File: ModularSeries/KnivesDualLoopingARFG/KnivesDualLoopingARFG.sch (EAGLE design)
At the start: 74 parts, among them P1 2XWIREPAD, P2 2XWIREPAD, P3 2XWIREPAD, P4 2XWIREPAD, Q1 2N3904, Q2 2N3904

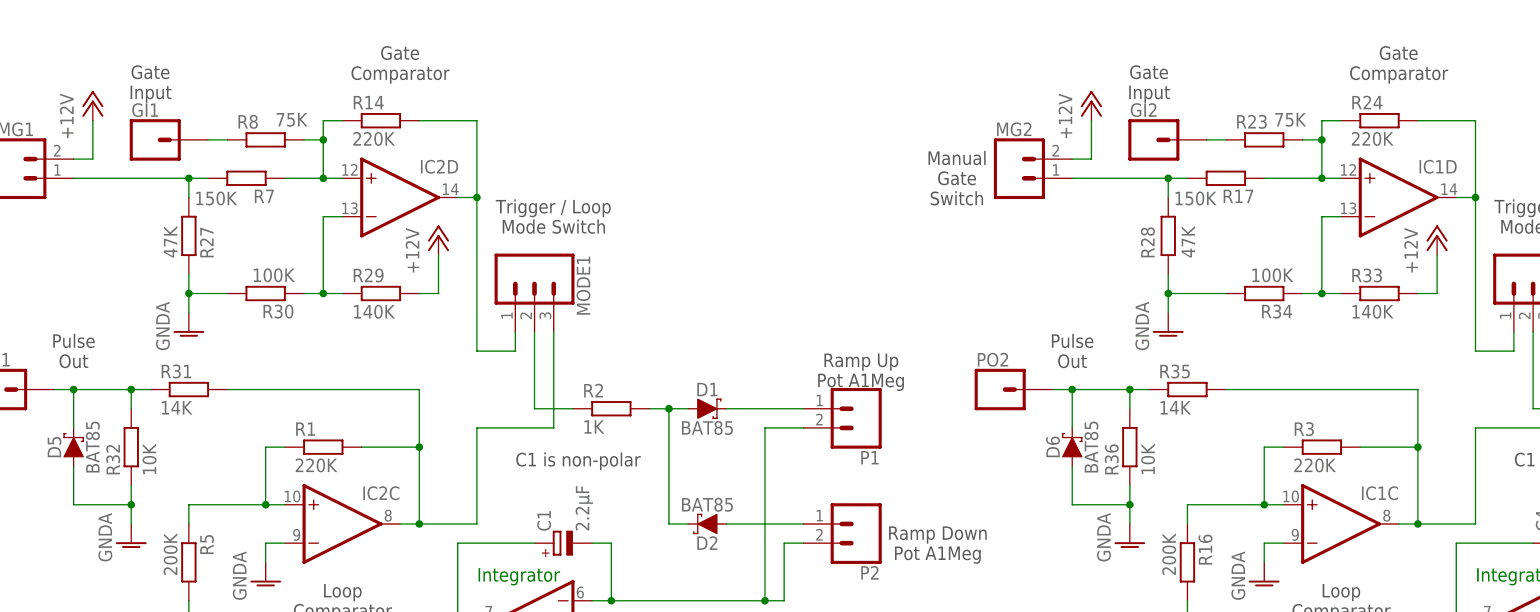
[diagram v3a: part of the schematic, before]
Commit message: Updates to Portals and Knives, Panel layout for Prism and Knives added
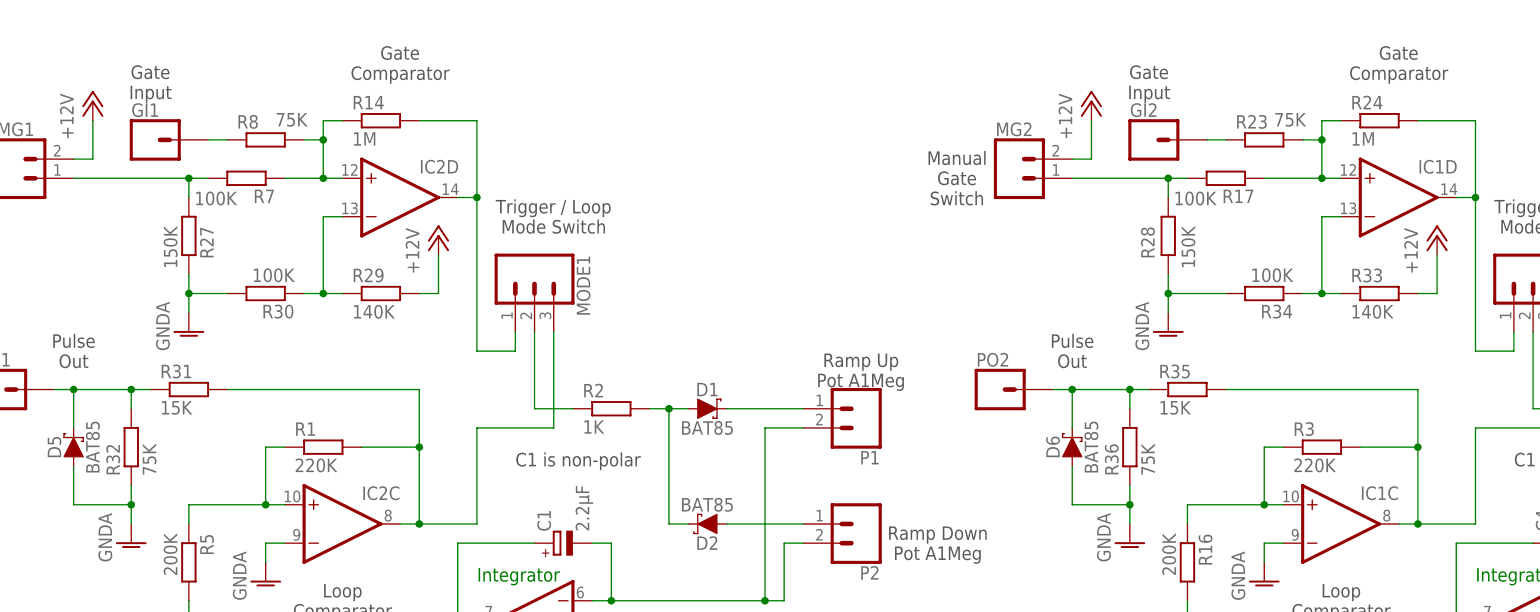
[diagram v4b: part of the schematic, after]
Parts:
- R14, R24: value 220K -> 1M
- R17, R7: value 150K -> 100K
- R27, R28: value 47K -> 150K
- R31, R35: value 14K -> 15K
- R32, R36: value 10K -> 75K
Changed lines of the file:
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@@
 <part name="R2" library="rcl" library_urn="urn:adsk.eagle:library:334" deviceset="R-EU_" device="0207/10" package3d_urn="urn:adsk.eagle:package:23491/2" value="1K"/>
 <part name="R5" library="rcl" library_urn="urn:adsk.eagle:library:334" deviceset="R-EU_" device="0207/10" package3d_urn="urn:adsk.eagle:package:23491/2" value="200K"/>
-<part name="R7" library="rcl" library_urn="urn:adsk.eagle:library:334" deviceset="R-EU_" device="0207/10" package3d_urn="urn:adsk.eagle:package:23491/2" value="150K"/>
+<part name="R7" library="rcl" library_urn="urn:adsk.eagle:library:334" deviceset="R-EU_" device="0207/10" package3d_urn="urn:adsk.eagle:package:23491/2" value="100K"/>
 <part name="R9" library="rcl" library_urn="urn:adsk.eagle:library:334" deviceset="R-EU_" device="0207/10" package3d_urn="urn:adsk.eagle:package:23491/2" value="100K"/>
 <part name="R10" library="rcl" library_urn="urn:adsk.eagle:library:334" deviceset="R-EU_" device="0207/10" package3d_urn="urn:adsk.eagle:package:23491/2" value="47K"/>
@@
 <part name="R8" library="rcl" library_urn="urn:adsk.eagle:library:334" deviceset="R-EU_" device="0207/10" package3d_urn="urn:adsk.eagle:package:23491/2" value="75K"/>
 <part name="P+2" library="supply1" library_urn="urn:adsk.eagle:library:371" deviceset="+12V" device=""/>
-<part name="R14" library="rcl" library_urn="urn:adsk.eagle:library:334" deviceset="R-EU_" device="0207/10" package3d_urn="urn:adsk.eagle:package:23491/2" value="220K"/>
+<part name="R14" library="rcl" library_urn="urn:adsk.eagle:library:334" deviceset="R-EU_" device="0207/10" package3d_urn="urn:adsk.eagle:package:23491/2" value="1M"/>
 <part name="Q1" library="transistor" library_urn="urn:adsk.eagle:library:402" deviceset="2N3904" device="" package3d_urn="urn:adsk.eagle:package:28523/2" value="2N3904"/>
 <part name="R6" library="rcl" library_urn="urn:adsk.eagle:library:334" deviceset="R-EU_" device="0207/10" package3d_urn="urn:adsk.eagle:package:23491/2" value="100Ω"/>
@@
 <part name="R4" library="rcl" library_urn="urn:adsk.eagle:library:334" deviceset="R-EU_" device="0207/10" package3d_urn="urn:adsk.eagle:package:23491/2" value="1K"/>
 <part name="R16" library="rcl" library_urn="urn:adsk.eagle:library:334" deviceset="R-EU_" device="0207/10" package3d_urn="urn:adsk.eagle:package:23491/2" value="200K"/>
-<part name="R17" library="rcl" library_urn="urn:adsk.eagle:library:334" deviceset="R-EU_" device="0207/10" package3d_urn="urn:adsk.eagle:package:23491/2" value="150K"/>
+<part name="R17" library="rcl" library_urn="urn:adsk.eagle:library:334" deviceset="R-EU_" device="0207/10" package3d_urn="urn:adsk.eagle:package:23491/2" value="100K"/>
 <part name="R18" library="rcl" library_urn="urn:adsk.eagle:library:334" deviceset="R-EU_" device="0207/10" package3d_urn="urn:adsk.eagle:package:23491/2" value="100K"/>
 <part name="R19" library="rcl" library_urn="urn:adsk.eagle:library:334" deviceset="R-EU_" device="0207/10" package3d_urn="urn:adsk.eagle:package:23491/2" value="47K"/>
@@
 <part name="R23" library="rcl" library_urn="urn:adsk.eagle:library:334" deviceset="R-EU_" device="0207/10" package3d_urn="urn:adsk.eagle:package:23491/2" value="75K"/>
 <part name="P+5" library="supply1" library_urn="urn:adsk.eagle:library:371" deviceset="+12V" device=""/>
-<part name="R24" library="rcl" library_urn="urn:adsk.eagle:library:334" deviceset="R-EU_" device="0207/10" package3d_urn="urn:adsk.eagle:package:23491/2" value="220K"/>
+<part name="R24" library="rcl" library_urn="urn:adsk.eagle:library:334" deviceset="R-EU_" device="0207/10" package3d_urn="urn:adsk.eagle:package:23491/2" value="1M"/>
 <part name="GND11" library="supply1" library_urn="urn:adsk.eagle:library:371" deviceset="GNDA" device=""/>
 <part name="Q2" library="transistor" library_urn="urn:adsk.eagle:library:402" deviceset="2N3904" device="" package3d_urn="urn:adsk.eagle:package:28523/2" value="2N3904"/>
@@
 <part name="H3" library="holes" library_urn="urn:adsk.eagle:library:237" deviceset="MOUNT-HOLE" device="3.2" package3d_urn="urn:adsk.eagle:package:14275/1"/>
 <part name="H4" library="holes" library_urn="urn:adsk.eagle:library:237" deviceset="MOUNT-HOLE" device="3.2" package3d_urn="urn:adsk.eagle:package:14275/1"/>
-<part name="R27" library="rcl" library_urn="urn:adsk.eagle:library:334" deviceset="R-EU_" device="0207/10" package3d_urn="urn:adsk.eagle:package:23491/2" value="47K"/>
-<part name="R28" library="rcl" library_urn="urn:adsk.eagle:library:334" deviceset="R-EU_" device="0207/10" package3d_urn="urn:adsk.eagle:package:23491/2" value="47K"/>
+<part name="R27" library="rcl" library_urn="urn:adsk.eagle:library:334" deviceset="R-EU_" device="0207/10" package3d_urn="urn:adsk.eagle:package:23491/2" value="150K"/>
+<part name="R28" library="rcl" library_urn="urn:adsk.eagle:library:334" deviceset="R-EU_" device="0207/10" package3d_urn="urn:adsk.eagle:package:23491/2" value="150K"/>
 <part name="PO1" library="ElectricNoodleBox" deviceset="1XWIREPAD" device=""/>
 <part name="PO2" library="ElectricNoodleBox" deviceset="1XWIREPAD" device=""/>
@@
 <attribute name="SPICEPREFIX" value="G"/>
 </part>
-<part name="R31" library="rcl" library_urn="urn:adsk.eagle:library:334" deviceset="R-EU_" device="0207/10" package3d_urn="urn:adsk.eagle:package:23491/2" value="14K"/>
-<part name="R32" library="rcl" library_urn="urn:adsk.eagle:library:334" deviceset="R-EU_" device="0207/10" package3d_urn="urn:adsk.eagle:package:23491/2" value="10K"/>
+<part name="R31" library="rcl" library_urn="urn:adsk.eagle:library:334" deviceset="R-EU_" device="0207/10" package3d_urn="urn:adsk.eagle:package:23491/2" value="15K"/>
+<part name="R32" library="rcl" library_urn="urn:adsk.eagle:library:334" deviceset="R-EU_" device="0207/10" package3d_urn="urn:adsk.eagle:package:23491/2" value="75K"/>
 <part name="GND15" library="supply1" library_urn="urn:adsk.eagle:library:371" deviceset="GNDA" device=""/>
 <part name="D5" library="ElectricNoodleBox" deviceset="SCHOTTKY_DO35" device="" package3d_urn="urn:adsk.eagle:package:43339/2" value="BAT85"/>
@@
 <part name="R33" library="rcl" library_urn="urn:adsk.eagle:library:334" deviceset="R-EU_" device="0207/10" package3d_urn="urn:adsk.eagle:package:23491/2" value="140K"/>
 <part name="R34" library="rcl" library_urn="urn:adsk.eagle:library:334" deviceset="R-EU_" device="0207/10" package3d_urn="urn:adsk.eagle:package:23491/2" value="100K"/>
-<part name="R35" library="rcl" library_urn="urn:adsk.eagle:library:334" deviceset="R-EU_" device="0207/10" package3d_urn="urn:adsk.eagle:package:23491/2" value="14K"/>
-<part name="R36" library="rcl" library_urn="urn:adsk.eagle:library:334" deviceset="R-EU_" device="0207/10" package3d_urn="urn:adsk.eagle:package:23491/2" value="10K"/>
+<part name="R35" library="rcl" library_urn="urn:adsk.eagle:library:334" deviceset="R-EU_" device="0207/10" package3d_urn="urn:adsk.eagle:package:23491/2" value="15K"/>
+<part name="R36" library="rcl" library_urn="urn:adsk.eagle:library:334" deviceset="R-EU_" device="0207/10" package3d_urn="urn:adsk.eagle:package:23491/2" value="75K"/>
 <part name="GND5" library="supply1" library_urn="urn:adsk.eagle:library:371" deviceset="GNDA" device=""/>
 <part name="D6" library="ElectricNoodleBox" deviceset="SCHOTTKY_DO35" device="" package3d_urn="urn:adsk.eagle:package:43339/2" value="BAT85"/>

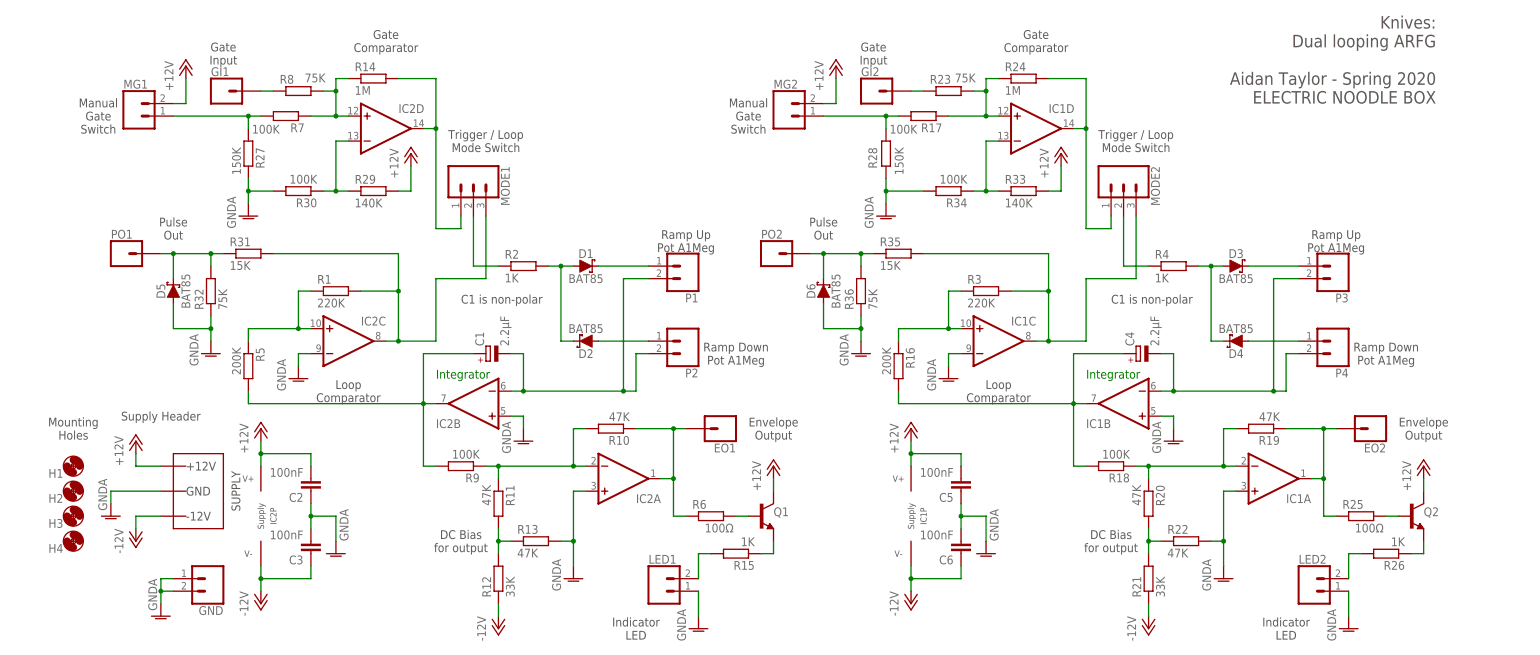
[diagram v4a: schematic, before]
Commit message: Pulse output fixed on Knives, schematics and layout updated. Panel added for Portals
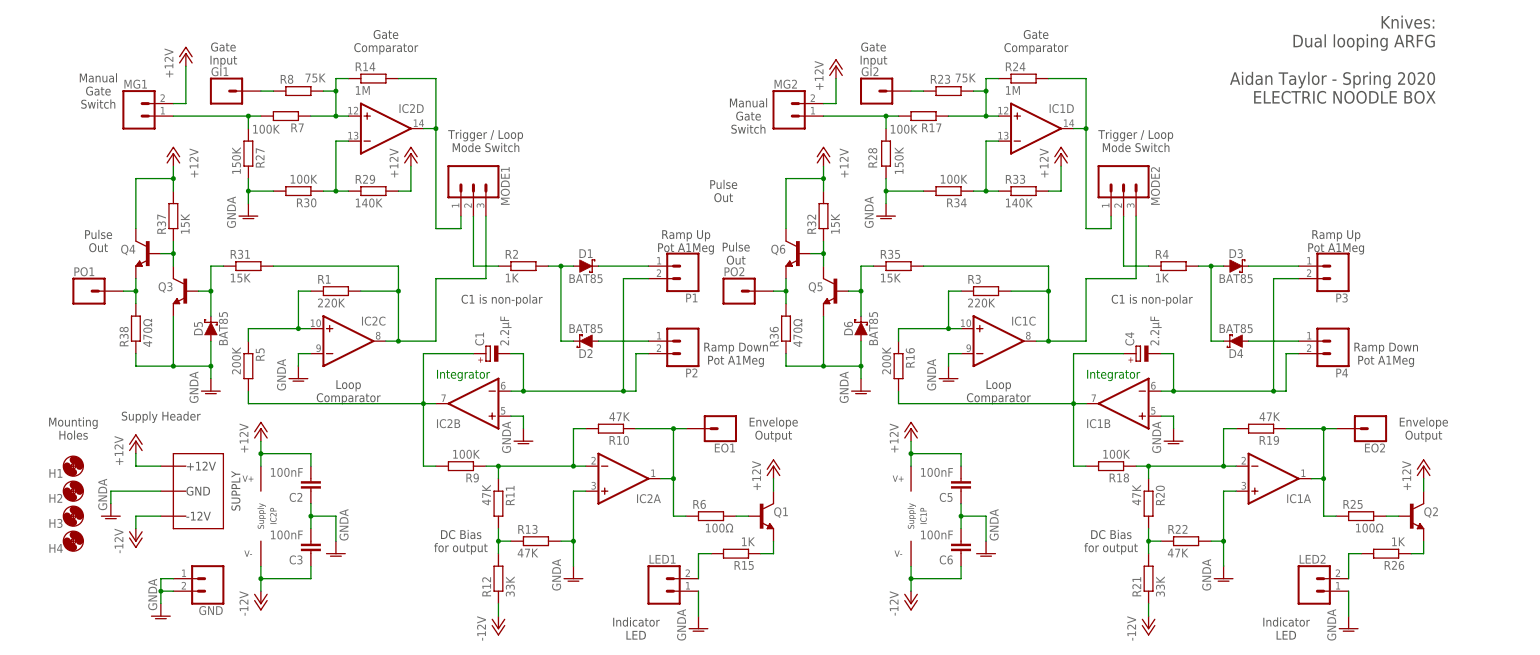
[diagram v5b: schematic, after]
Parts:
- added Q3, Q4, Q5, Q6: 2N3904, transistor:2N3904
- added R37: 15K, rcl:R-EU_0207/10
- added R38: 470Ω, rcl:R-EU_0207/10
- R32: value 75K -> 15K
- R36: value 75K -> 470Ω
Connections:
- new net N$1: Q5.C, Q6.B, R32.1
- new net N$37: Q3.C, Q4.B, R37.1
- new net N$38: PO1.1, Q4.E, R38.2
- new net N$40: PO2.1, Q6.E, R36.2
- net +12V: now also Q4.C, Q6.C, R32.2, R37.2
- net GNDA: now also Q3.E, Q5.E, R38.1; no longer R32.1
- net N$34: now also Q3.B; no longer PO1.1, R32.2
- net N$36: now also Q5.B; no longer PO2.1, R36.2
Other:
- moved on the sheet: D5, D6, PO1, PO2, R31, R32, R35, R36

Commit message: Common collector + emitter follower pulse output added to Knives, docs updated
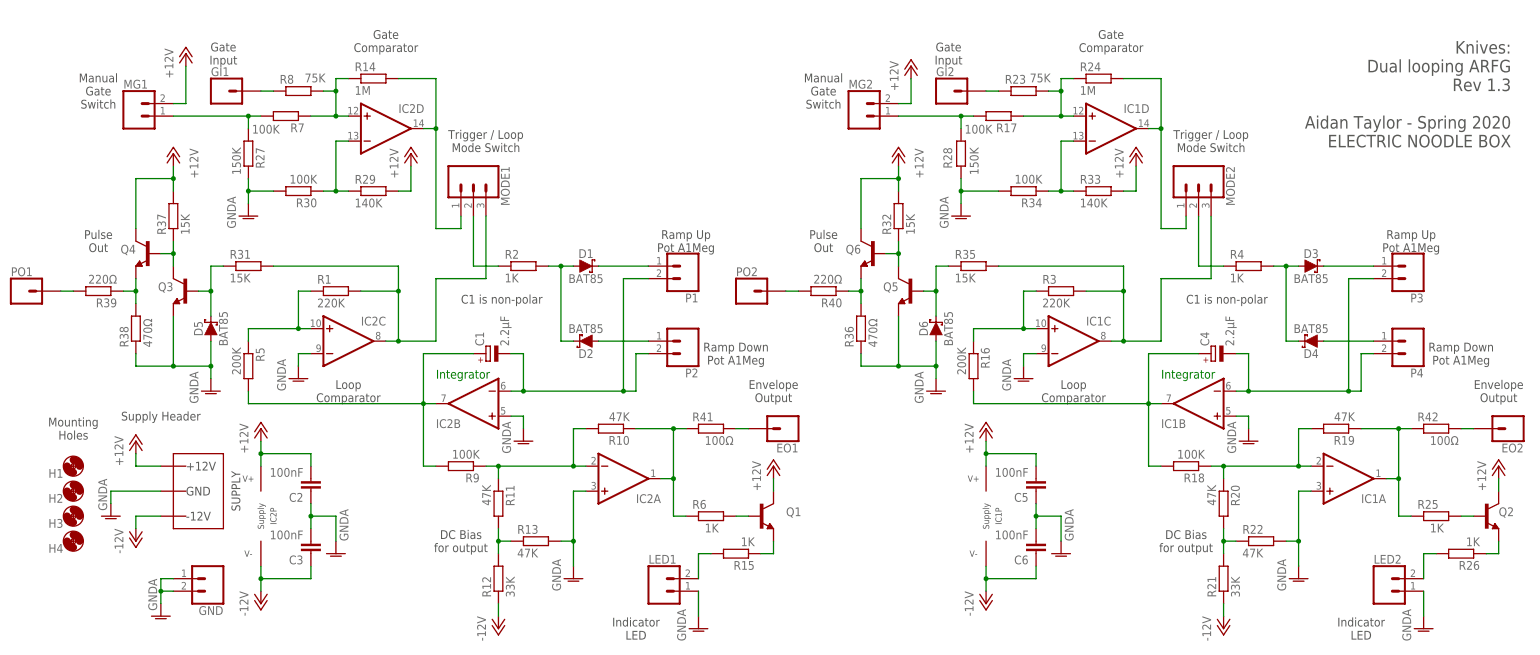
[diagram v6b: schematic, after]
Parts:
- added R39, R40: 220Ω, rcl:R-EU_0207/10
- added R41, R42: 100Ω, rcl:R-EU_0207/10
- R25, R6: value 100Ω -> 1K
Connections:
- new net N$41: PO1.1, R39.2
- new net N$42: PO2.1, R40.2
- new net N$43: EO1.1, R41.2
- new net N$44: EO2.1, R42.2
- net ENVELOPE_OUTPUT: now also R41.1; no longer EO1.1
- net ENVELOPE_OUTPUT1: now also R42.1; no longer EO2.1
- net N$38: now also R39.1; no longer PO1.1
- net N$40: now also R40.1; no longer PO2.1
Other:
- note added: "Knives: Dual looping ARFG Rev 1.3 Aidan Taylor - Spring 2020 ELECTRIC NOODLE BOX"
- note removed: "Knives: Dual looping ARFG Aidan Taylor - Spring 2020 ELECTRIC NOODLE BOX"
- moved on the sheet: C4, C5, C6, D3, D4, D6, EO1, EO2, GI2, IC1A, IC1B, IC1C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

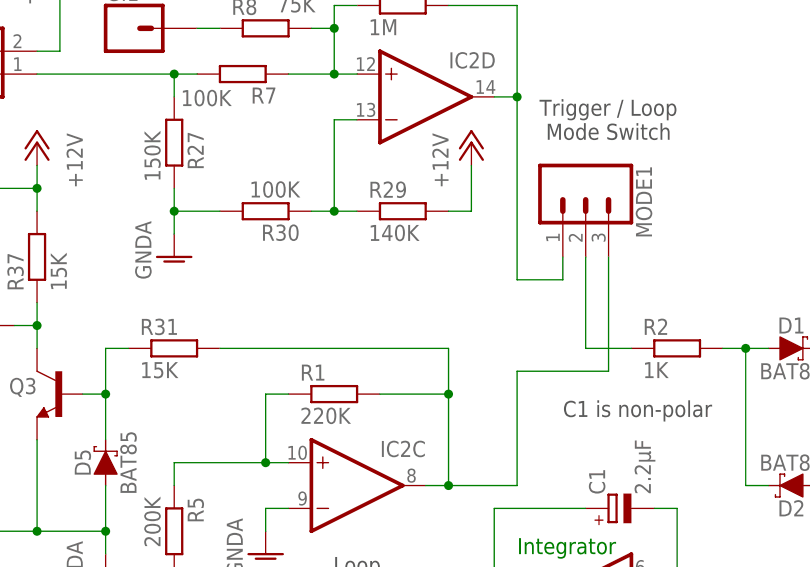
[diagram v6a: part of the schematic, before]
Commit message: Left Hand Path Project added, Core, Control and Panel Cards
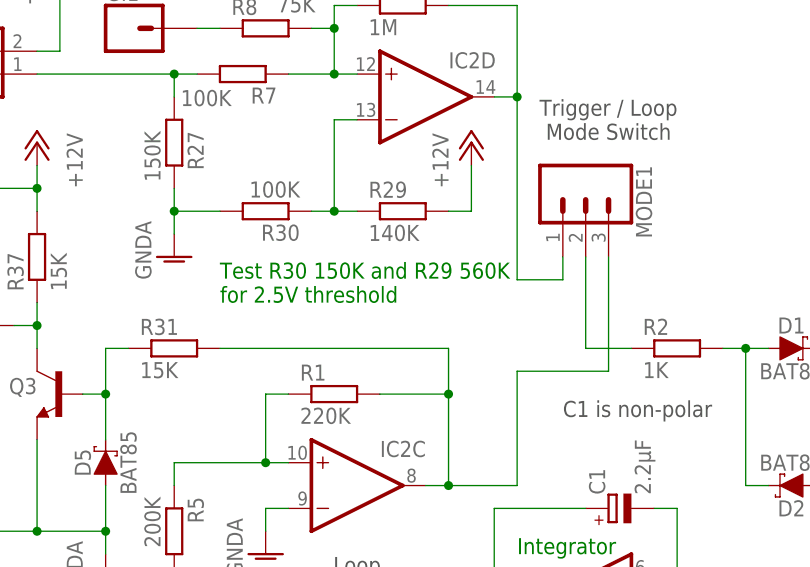
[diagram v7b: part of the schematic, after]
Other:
- note added: "Test R30 150K and R29 560K for 2.5V threshold"
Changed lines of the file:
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@@
 <?xml version="1.0" encoding="utf-8"?>
 <!DOCTYPE eagle SYSTEM "eagle.dtd">
-<eagle version="9.6.0">
+<eagle version="9.6.2">
 <drawing>
 <settings>
@@
 <text x="149.86" y="88.9" size="1.778" layer="97" align="center">Pulse
 Out</text>
+<text x="38.1" y="88.9" size="1.778" layer="91">Test R30 150K and R29 560K
+for 2.5V threshold</text>
 </plain>
 <instances>
